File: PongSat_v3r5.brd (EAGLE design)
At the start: 39.1 x 39.2 mm, 35 parts, among them U1 MIC5129 3v3, U2 Micro SD, X1 USB-MICROB, Y1 8MHz

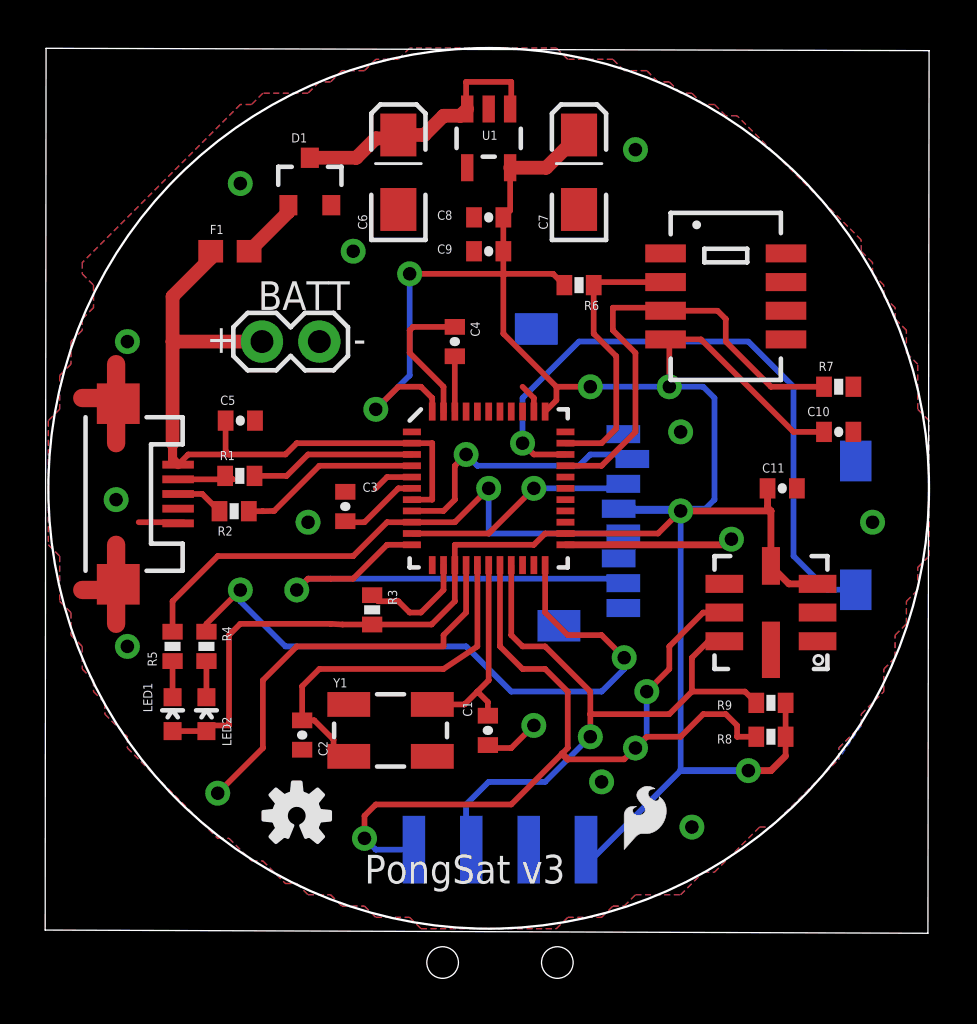
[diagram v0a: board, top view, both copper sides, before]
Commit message: Updated to Version 3 Revision 5
I2C header is now PTH, and various other slight tweaks have been
applied. New Gerber filed also committed. Directory structure also
simplified and reorganised.
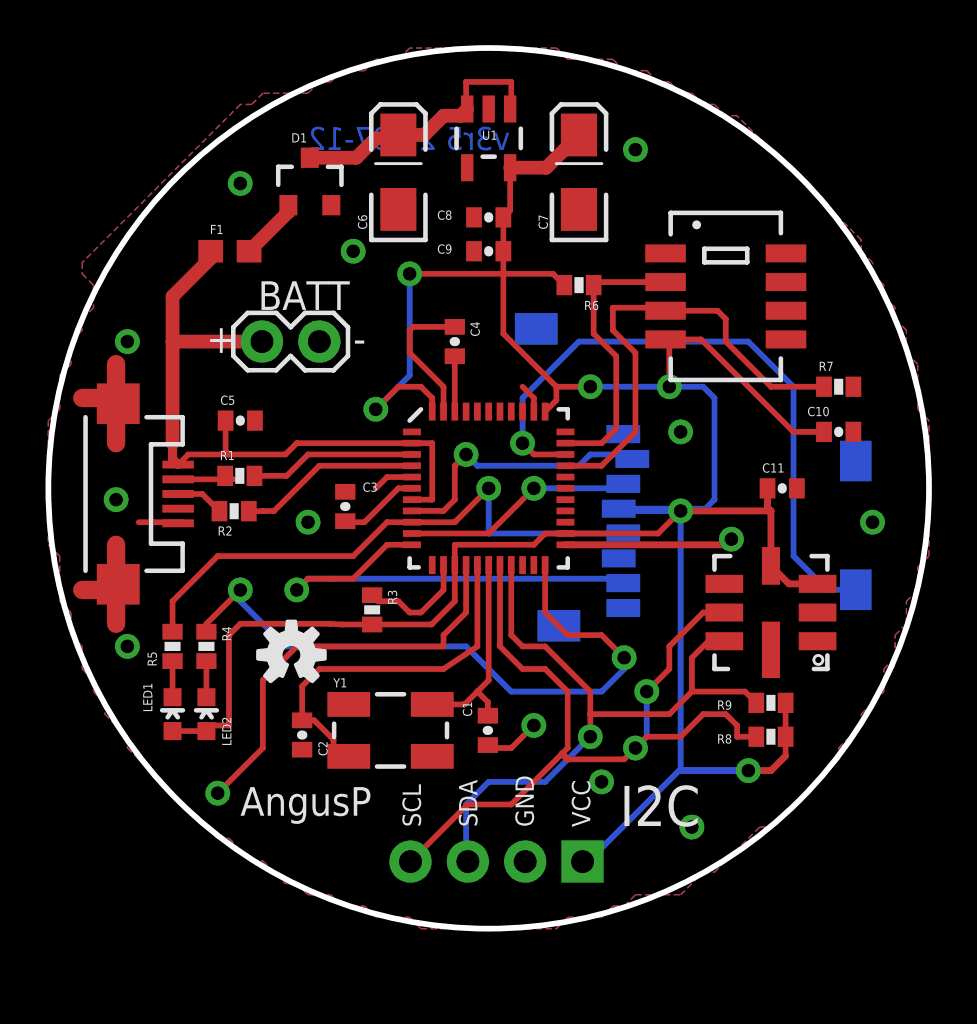
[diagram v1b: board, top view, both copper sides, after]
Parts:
- removed U$2: (no value), SparkFun-Aesthetics:SFE-LOGO-FLAME
- I2C: device SparkFun-Connectors:1X04-SMD -> SparkFun-Connectors:1X04
- moved U$1 7.13 mm to (10.8, 12.1)
- moved I2C 5.78 mm to (23.7, 2.97)
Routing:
- net SCL: track 42.3 -> 37.4 mm, vias 3 -> 2
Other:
- board size 39.1 x 39.2 mm -> 39 x 39 mm
- board text added: "AngusP"
- board text added: "v3r5 29-07-12"
- board text removed: "PongSat v3"
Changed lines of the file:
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@@
 <board>
 <plain>
-<wire x1="-0.142" y1="-0.062" x2="38.952" y2="-0.204" width="0" layer="20"/>
-<wire x1="38.952" y1="-0.204" x2="39.004" y2="38.884" width="0" layer="20"/>
-<wire x1="39.004" y1="38.884" x2="-0.102" y2="38.988" width="0" layer="20"/>
-<wire x1="-0.102" y1="38.988" x2="-0.142" y2="-0.062" width="0" layer="20"/>
-<circle x="19.5" y="19.5" radius="19.5" width="0.1" layer="20"/>
-<text x="19.5" y="8.5" size="1.778" layer="22" rot="MR0">I2C</text>
-<text x="14" y="2" size="1.27" layer="21">PongSat v3</text>
+<circle x="19.5" y="19.5" radius="19.5" width="0.254" layer="20"/>
+<text x="25.2992" y="4.5456" size="1.778" layer="21">I2C</text>
 <text x="7" y="25.5" size="1.27" layer="21">+</text>
 <text x="13.5" y="25.5" size="1.27" layer="21">-</text>
-<text x="24" y="5.5" size="0.8128" layer="22" rot="R90">VCC</text>
-<text x="21.5" y="5.5" size="0.8128" layer="22" rot="R90">GND</text>
-<text x="19" y="5.5" size="0.8128" layer="22" rot="R90">SDA</text>
-<text x="16.5" y="5.5" size="0.8128" layer="22" rot="R90">SCL</text>
+<text x="23" y="4.5" size="0.8128" layer="22" rot="MR90">VCC</text>
+<text x="20.5" y="4.5" size="0.8128" layer="22" rot="MR90">GND</text>
+<text x="18" y="4.5" size="0.8128" layer="22" rot="MR90">SDA</text>
+<text x="15.5" y="4.5" size="0.8128" layer="22" rot="MR90">SCL</text>
+<text x="24" y="4.5" size="0.8128" layer="21" ratio="7" rot="R90">VCC</text>
+<text x="21.5" y="4.5" size="0.8128" layer="21" ratio="7" rot="R90">GND</text>
+<text x="19" y="4.5" size="0.8128" layer="21" ratio="7" rot="R90">SDA</text>
+<text x="16.5" y="4.5" size="0.8128" layer="21" ratio="7" rot="R90">SCL</text>
+<text x="11.5" y="35.5" size="1.016" layer="16" ratio="7" rot="MR180">v3r5 29-07-12</text>
+<text x="8.5" y="5" size="1.27" layer="21" ratio="11">AngusP</text>
 </plain>
 <attributes>
@@
 <attribute name="VALUE" x="29.15" y="28.58" size="0.8128" layer="22" rot="MR180"/>
 </element>
-<element name="I2C" library="SparkFun-Connectors" package="1X04-SMD" value="3.3V" x="20" y="-1.5" locked="yes" smashed="yes" rot="MR0"/>
-<element name="U$1" library="SparkFun-Aesthetics" package="OSHW-LOGO-S" value="" x="11" y="5"/>
-<element name="U$2" library="SparkFun-Aesthetics" package="SFE-LOGO-FLAME" value="" x="25.5" y="3.5"/>
+<element name="I2C" library="SparkFun-Connectors" package="1X04" value="3.3V" x="23.6576" y="2.9704" locked="yes" smashed="yes" rot="MR0"/>
+<element name="U$1" library="SparkFun-Aesthetics" package="OSHW-LOGO-S" value="" x="10.7648" y="12.1256"/>
 <element name="SHT" library="SparkFun-Sensors" package="SHT1X" value="SHT1XSMD" x="30" y="28" locked="yes" smashed="yes"/>
 <element name="C10" library="SparkFun-Passives" package="0402-CAP" value="0.1uF" x="35" y="22" smashed="yes">
@@
 <wire x1="22" y1="6.5" x2="19.5" y2="6.5" width="0.254" layer="16"/>
 <wire x1="19.5" y1="6.5" x2="18.5" y2="5.5" width="0.254" layer="16"/>
-<wire x1="18.5" y1="5.5" x2="18.5" y2="3.73" width="0.254" layer="16"/>
-<wire x1="18.5" y1="3.73" x2="18.73" y2="3.5" width="0.254" layer="16"/>
 <contactref element="BMP" pad="7"/>
 <wire x1="29.935" y1="12.73" x2="29.23" y2="12.73" width="0.254" layer="1"/>
@@
 <wire x1="31.35" y1="10" x2="30.85" y2="10.5" width="0.254" layer="1"/>
 <wire x1="30.85" y1="10.5" x2="28.5" y2="10.5" width="0.254" layer="1"/>
+<wire x1="18.5" y1="5.5" x2="18.5" y2="3.048" width="0.254" layer="16"/>
+<wire x1="18.5" y1="3.048" x2="18.5776" y2="2.9704" width="0.254" layer="16"/>
 </signal>
 <signal name="SCL">
@@
 <wire x1="23" y1="8" x2="22.75" y2="7.75" width="0.254" layer="1"/>
 <wire x1="22.75" y1="7.75" x2="20.5" y2="5.5" width="0.254" layer="1"/>
-<wire x1="20.5" y1="5.5" x2="14.5" y2="5.5" width="0.254" layer="1"/>
-<wire x1="14.5" y1="5.5" x2="14" y2="5" width="0.254" layer="1"/>
-<wire x1="14" y1="5" x2="14" y2="4" width="0.254" layer="1"/>
-<via x="14" y="4" extent="1-16" drill="0.6"/>
-<wire x1="14" y1="4" x2="14.5" y2="3.5" width="0.254" layer="16"/>
-<wire x1="14.5" y1="3.5" x2="16.19" y2="3.5" width="0.254" layer="16"/>
 <wire x1="22" y1="11.5" x2="23" y2="10.5" width="0.254" layer="1"/>
 <wire x1="23" y1="10.5" x2="23" y2="8" width="0.254" layer="1"/>
-<wire x1="16" y1="3.69" x2="16.19" y2="3.5" width="0.254" layer="16"/>
 <contactref element="BMP" pad="6"/>
 <wire x1="29.935" y1="14" x2="29" y2="14" width="0.254" layer="1"/>
@@
 <wire x1="28" y1="8.5" x2="26.5" y2="8.5" width="0.254" layer="1"/>
 <wire x1="26.5" y1="8.5" x2="26" y2="8" width="0.254" layer="1"/>
+<wire x1="20.5" y1="5.5" x2="18.5672" y2="5.5" width="0.254" layer="1"/>
+<wire x1="18.5672" y1="5.5" x2="16.0376" y2="2.9704" width="0.254" layer="1"/>
 </signal>
 <signal name="TXO">
@@
 <wire x1="16" y1="29" x2="20.15" y2="29" width="0.254" layer="1"/>
 <contactref element="I2C" pad="1"/>
-<wire x1="23.81" y1="3.5" x2="24" y2="3" width="0.254" layer="16"/>
-<wire x1="24" y1="3" x2="28" y2="7" width="0.254" layer="16"/>
 <wire x1="28" y1="7" x2="28" y2="18.5" width="0.254" layer="16"/>
 <wire x1="14.34" y1="13.47" x2="13.03" y2="13.47" width="0.254" layer="1"/>
@@
 <wire x1="22.85" y1="28.5" x2="22.35" y2="29" width="0.254" layer="1"/>
 <wire x1="22.35" y1="29" x2="20.15" y2="29" width="0.254" layer="1"/>
+<wire x1="28" y1="7" x2="27.9296" y2="7" width="0.254" layer="16"/>
+<wire x1="27.9296" y1="7" x2="23.9" y2="2.9704" width="0.254" layer="16"/>
+<wire x1="23.9" y1="2.9704" x2="23.6576" y2="2.9704" width="0.254" layer="16"/>
 </signal>
 <signal name="CS">
